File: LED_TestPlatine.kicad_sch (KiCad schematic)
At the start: 1 part, among them Y1 XEGARY-H2-0000-000-000000K2001

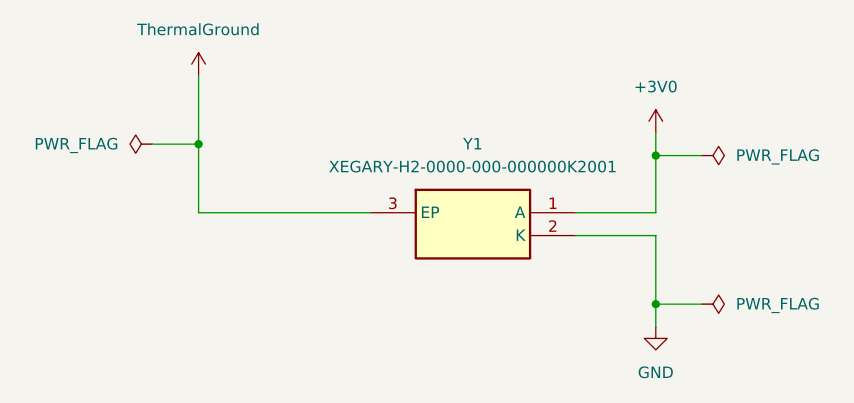
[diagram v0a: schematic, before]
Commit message: added resistor to respective files
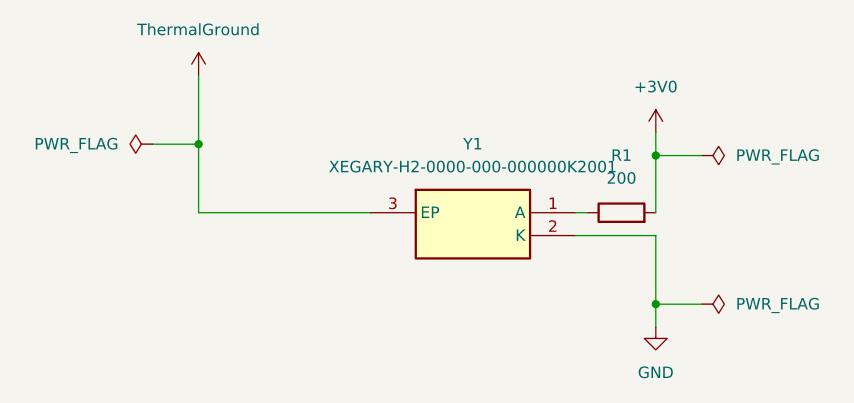
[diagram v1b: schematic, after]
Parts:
- added R1: 200, Resistor_SMD:R_01005_0402Metric, symbol Device:R
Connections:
- net +3V0: now also R1.2; no longer Y1.1 (A)
- new net: R1.1, Y1.1 (A)
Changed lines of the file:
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@@
 	(wire
 		(pts
-			(xy 168.91 91.44) (xy 177.8 91.44)
+			(xy 168.91 91.44) (xy 170.18 91.44)
 		)
 		(stroke
@@
 					(unit 1)
 				)
+			)
+		)
+	)
+	(symbol
+		(lib_id "Device:R")
+		(at 173.99 91.44 90)
+		(unit 1)
+		(body_style 1)
+		(exclude_from_sim no)
+		(in_bom yes)
+		(on_board yes)
+		(in_pos_files yes)
+		(dnp no)
+		(fields_autoplaced yes)
+		(property "Reference" "R1"
+			(at 173.99 85.09 90)
+			(show_name no)
+			(do_not_autoplace no)
+			(effects
+				(font
+					(size 1.27 1.27)
+				)
+			)
+		)
+		(property "Value" "200"
+			(at 173.99 87.63 90)
+			(show_name no)
+			(do_not_autoplace no)
+			(effects
+				(font
+					(size 1.27 1.27)
+				)
+			)
+		)
+		(property "Footprint" "Resistor_SMD:R_01005_0402Metric"
+			(at 173.99 93.218 90)
+			(hide yes)
+			(show_name no)
+			(do_not_autoplace no)
+			(effects
+				(font
+					(size 1.27 1.27)
+				)
+			)
+		)
+		(property "Datasheet" ""
+			(at 173.99 91.44 0)
+			(hide yes)
+			(show_name no)
+			(do_not_autoplace no)
+			(effects
+				(font
+					(size 1.27 1.27)
+				)
+			)
+		)
+		(property "Description" "Resistor"
+			(at 173.99 91.44 0)
+			(hide yes)
+			(show_name no)
+			(do_not_autoplace no)
+			(effects
+				(font
+					(size 1.27 1.27)
+				)
+			)
+		)
+		(pin "1"
+		)
+		(pin "2"
+		)
+		(instances
+			(project "LED_TestPlatine_mit_R"
+				(path "/9579e0b5-2a8a-4151-af14-715dc76a141a"
+					(reference "R1")
+					(unit 1)
+				)

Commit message: moved resistor to the correct board file
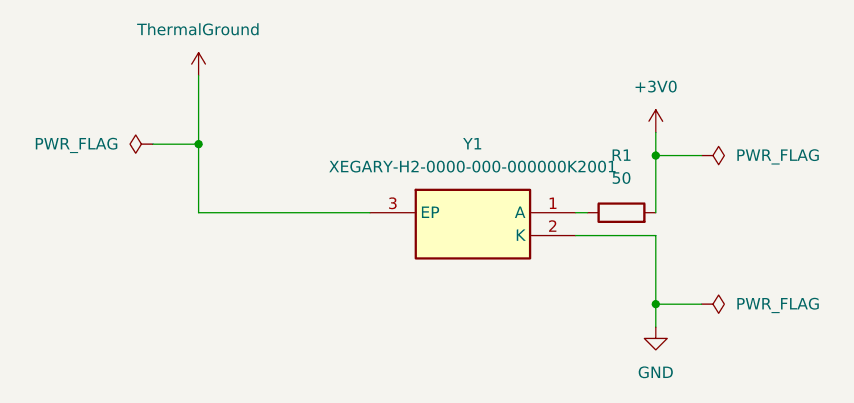
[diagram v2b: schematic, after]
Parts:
- R1: value 200 -> 50; footprint Resistor_SMD:R_01005_0402Metric -> Resistor_SMD:R_0201_0603Metric
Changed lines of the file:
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@@
+	)
+	(symbol
+		(lib_id "Device:R")
+		(at 173.99 91.44 90)
+		(unit 1)
+		(body_style 1)
+		(exclude_from_sim no)
+		(in_bom yes)
+		(on_board yes)
+		(in_pos_files yes)
+		(dnp no)
+		(fields_autoplaced yes)
+		(property "Reference" "R1"
+			(at 173.99 85.09 90)
+			(show_name no)
+			(do_not_autoplace no)
+			(effects
+				(font
+					(size 1.27 1.27)
+				)
+			)
+		)
+		(property "Value" "50"
+			(at 173.99 87.63 90)
+			(show_name no)
+			(do_not_autoplace no)
+			(effects
+				(font
+					(size 1.27 1.27)
+				)
+			)
+		)
+		(property "Footprint" "Resistor_SMD:R_0201_0603Metric"
+			(at 173.99 93.218 90)
+			(hide yes)
+			(show_name no)
+			(do_not_autoplace no)
+			(effects
+				(font
+					(size 1.27 1.27)
+				)
+			)
+		)
+		(property "Datasheet" ""
+			(at 173.99 91.44 0)
+			(hide yes)
+			(show_name no)
+			(do_not_autoplace no)
+			(effects
+				(font
+					(size 1.27 1.27)
+				)
+			)
+		)
+		(property "Description" "Resistor"
+			(at 173.99 91.44 0)
+			(hide yes)
+			(show_name no)
+			(do_not_autoplace no)
+			(effects
+				(font
+					(size 1.27 1.27)
+				)
+			)
+		)
+		(pin "1"
+		)
+		(pin "2"
+		)
+		(instances
+			(project "LED_TestPlatine_mit_R"
+				(path "/9579e0b5-2a8a-4151-af14-715dc76a141a"
+					(reference "R1")
+					(unit 1)
+				)
+			)
+		)
 	)
 	(symbol
@@
 					(unit 1)
 				)
-			)
-		)
-	)
-	(symbol
-		(lib_id "Device:R")
-		(at 173.99 91.44 90)
-		(unit 1)
-		(body_style 1)
-		(exclude_from_sim no)
-		(in_bom yes)
-		(on_board yes)
-		(in_pos_files yes)
-		(dnp no)
-		(fields_autoplaced yes)
-		(property "Reference" "R1"
-			(at 173.99 85.09 90)
-			(show_name no)
-			(do_not_autoplace no)
-			(effects
-				(font
-					(size 1.27 1.27)
-				)
-			)
-		)
-		(property "Value" "200"
-			(at 173.99 87.63 90)
-			(show_name no)
-			(do_not_autoplace no)
-			(effects
-				(font
-					(size 1.27 1.27)
-				)
-			)
-		)
-		(property "Footprint" "Resistor_SMD:R_01005_0402Metric"
-			(at 173.99 93.218 90)
-			(hide yes)
-			(show_name no)
-			(do_not_autoplace no)
-			(effects
-				(font
-					(size 1.27 1.27)
-				)
-			)
-		)
-		(property "Datasheet" ""
-			(at 173.99 91.44 0)
-			(hide yes)
-			(show_name no)
-			(do_not_autoplace no)
-			(effects
-				(font
-					(size 1.27 1.27)
-				)
-			)
-		)
-		(property "Description" "Resistor"
-			(at 173.99 91.44 0)
-			(hide yes)
-			(show_name no)
-			(do_not_autoplace no)
-			(effects
-				(font
-					(size 1.27 1.27)
-				)
-			)
-		)
-		(pin "1"
-		)
-		(pin "2"
-		)
-		(instances
-			(project "LED_TestPlatine_mit_R"
-				(path "/9579e0b5-2a8a-4151-af14-715dc76a141a"
-					(reference "R1")
-					(unit 1)
-				)
